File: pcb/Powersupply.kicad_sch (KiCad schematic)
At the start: 37 parts, among them IC3 UCC28910DR, Q3 HL3401A, U3 TPS54202DDC

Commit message: changed capacitors and resistors footprints from 0201 to 0603
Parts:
- C13, C14, C17, C20, C21, C22, C23, C24, C25: footprint Capacitor_SMD:C_0201_0603Metric -> Capacitor_SMD:C_0603_1608Metric
- R16, R17, R23, R24, R26, R27, R33, R34, R35, R36, R37: footprint Resistor_SMD:R_0201_0603Metric -> Resistor_SMD:R_0603_1608Metric
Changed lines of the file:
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@@
 			)
 		)
-		(property "Footprint" "Capacitor_SMD:C_0201_0603Metric"
+		(property "Footprint" "Capacitor_SMD:C_0603_1608Metric"
 			(at 68.2752 163.83 0)
 			(effects
@@
 			)
 		)
-		(property "Footprint" "Capacitor_SMD:C_0201_0603Metric"
+		(property "Footprint" "Capacitor_SMD:C_0603_1608Metric"
 			(at 152.0952 166.37 0)
 			(effects
@@
 			)
 		)
-		(property "Footprint" "Resistor_SMD:R_0201_0603Metric"
+		(property "Footprint" "Resistor_SMD:R_0603_1608Metric"
 			(at 76.962 172.72 90)
 			(effects
@@
 			)
 		)
-		(property "Footprint" "Resistor_SMD:R_0201_0603Metric"
+		(property "Footprint" "Resistor_SMD:R_0603_1608Metric"
 			(at 26.67 160.782 90)
 			(effects
@@
 			)
 		)
-		(property "Footprint" "Resistor_SMD:R_0201_0603Metric"
+		(property "Footprint" "Resistor_SMD:R_0603_1608Metric"
 			(at 76.962 160.02 90)
 			(effects
@@
 			)
 		)
-		(property "Footprint" "Resistor_SMD:R_0201_0603Metric"
+		(property "Footprint" "Resistor_SMD:R_0603_1608Metric"
 			(at 98.552 96.52 90)
 			(effects
@@
 			)
 		)
-		(property "Footprint" "Capacitor_SMD:C_0201_0603Metric"
+		(property "Footprint" "Capacitor_SMD:C_0603_1608Metric"
 			(at 159.7152 176.53 0)
 			(effects
@@
 			)
 		)
-		(property "Footprint" "Resistor_SMD:R_0201_0603Metric"
+		(property "Footprint" "Resistor_SMD:R_0603_1608Metric"
 			(at 165.862 172.72 90)
 			(effects
@@
 			)
 		)
-		(property "Footprint" "Resistor_SMD:R_0201_0603Metric"
+		(property "Footprint" "Resistor_SMD:R_0603_1608Metric"
 			(at 165.862 162.56 90)
 			(effects
@@
 			)
 		)
-		(property "Footprint" "Resistor_SMD:R_0201_0603Metric"
+		(property "Footprint" "Resistor_SMD:R_0603_1608Metric"
 			(at 165.862 182.88 90)
 			(effects
@@
 			)
 		)
-		(property "Footprint" "Resistor_SMD:R_0201_0603Metric"
+		(property "Footprint" "Resistor_SMD:R_0603_1608Metric"
 			(at 29.972 167.64 90)
 			(effects
@@
 			)
 		)
-		(property "Footprint" "Capacitor_SMD:C_0201_0603Metric"
+		(property "Footprint" "Capacitor_SMD:C_0603_1608Metric"
 			(at 121.92 152.7048 0)
 			(effects
@@
 			)
 		)
-		(property "Footprint" "Capacitor_SMD:C_0201_0603Metric"
+		(property "Footprint" "Capacitor_SMD:C_0603_1608Metric"
 			(at 58.1152 163.83 0)
 			(effects
@@
 			)
 		)
-		(property "Footprint" "Capacitor_SMD:C_0201_0603Metric"
+		(property "Footprint" "Capacitor_SMD:C_0603_1608Metric"
 			(at 162.2552 77.47 0)
 			(effects
@@
 			)
 		)
-		(property "Footprint" "Resistor_SMD:R_0201_0603Metric"
+		(property "Footprint" "Resistor_SMD:R_0603_1608Metric"
 			(at 182.372 72.39 90)
 			(effects
@@
 			)
 		)
-		(property "Footprint" "Capacitor_SMD:C_0201_0603Metric"
+		(property "Footprint" "Capacitor_SMD:C_0603_1608Metric"
 			(at 140.6652 166.37 0)
 			(effects
@@
 			)
 		)
-		(property "Footprint" "Resistor_SMD:R_0201_0603Metric"
+		(property "Footprint" "Resistor_SMD:R_0603_1608Metric"
 			(at 223.012 95.25 90)
 			(effects
@@
 			)
 		)
-		(property "Footprint" "Capacitor_SMD:C_0201_0603Metric"
+		(property "Footprint" "Capacitor_SMD:C_0603_1608Metric"
 			(at 201.6252 99.06 0)
 			(effects
@@
 			)
 		)
-		(property "Footprint" "Resistor_SMD:R_0201_0603Metric"
+		(property "Footprint" "Resistor_SMD:R_0603_1608Metric"
 			(at 182.372 55.88 90)
 			(effects
@@
 			)
 		)
-		(property "Footprint" "Capacitor_SMD:C_0201_0603Metric"
+		(property "Footprint" "Capacitor_SMD:C_0603_1608Metric"
 			(at 169.8752 77.47 0)
 			(effects

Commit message: changed SCR drives to pnp drive and started schematic revision
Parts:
- C14: footprint Capacitor_SMD:C_0603_1608Metric -> Capacitor_THT:CP_Radial_D8.0mm_P5.00mm
- C19: footprint Capacitor_SMD:CP_Elec_3x5.4 -> Capacitor_THT:CP_Radial_D8.0mm_P5.00mm
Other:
- note removed: "Aggiungere filtro PiGreco usare calcolatore online"
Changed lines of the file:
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@@
 		)
 	)
-	(text "Aggiungere filtro PiGreco\nusare calcolatore online\n"
-		(exclude_from_sim no)
-		(at 82.296 77.47 0)
-		(effects
-			(font
-				(size 1.27 1.27)
-			)
-		)
-	)
 	(text "simulation"
 		(exclude_from_sim yes)
@@
 			)
 		)
-		(property "Footprint" "Capacitor_SMD:C_0603_1608Metric"
+		(property "Footprint" "Capacitor_THT:CP_Radial_D8.0mm_P5.00mm"
 			(at 162.2552 77.47 0)
 			(effects
@@
 			)
 		)
-		(property "Footprint" "Capacitor_SMD:CP_Elec_3x5.4"
+		(property "Footprint" "Capacitor_THT:CP_Radial_D8.0mm_P5.00mm"
 			(at 214.3252 99.06 0)
 			(effects

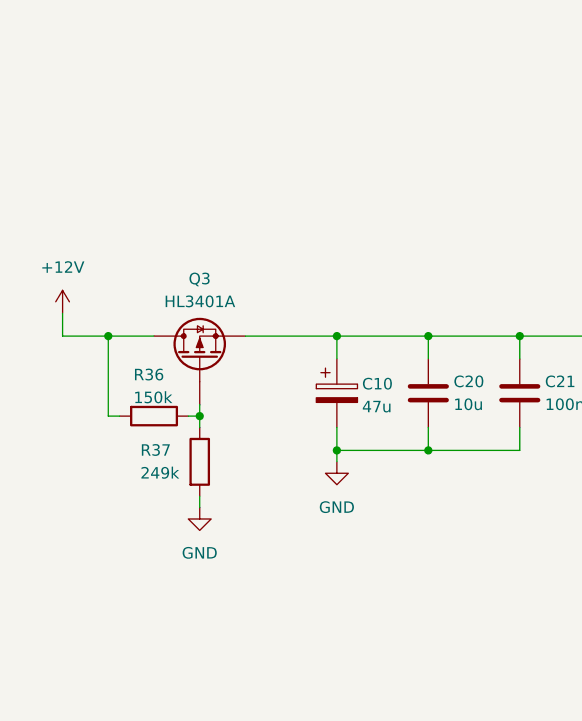
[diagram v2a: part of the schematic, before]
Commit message: fixed reverse polarity protection
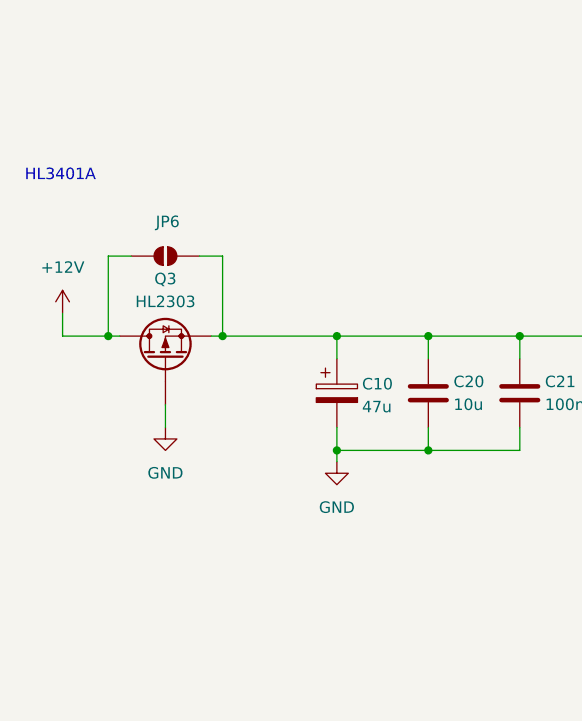
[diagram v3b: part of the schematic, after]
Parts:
- removed R36: 150k, Resistor_SMD:R_0603_1608Metric, symbol Device:R
- removed R37: 249k, Resistor_SMD:R_0603_1608Metric, symbol Device:R
- added JP6: SolderJumper_2_Open, Jumper:SolderJumper-2_P1.3mm_Open_RoundedPad1.0x1.5mm, symbol Jumper:SolderJumper_2_Open
- C10: footprint Capacitor_SMD:CP_Elec_3x5.4 -> Capacitor_THT:CP_Radial_D8.0mm_P5.00mm
- Q3: value HL3401A -> HL2303
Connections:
- net +12V: now also JP6.1 (A)
- net GND: now also Q3.1 (G)
- net at C10.1, C20.1, C21.1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: now also JP6.2 (B)
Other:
- note added: "HL3401A"
- moved on the sheet: Q3

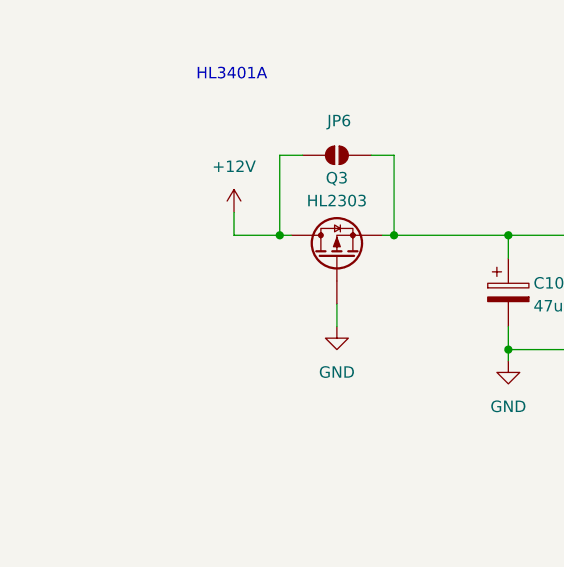
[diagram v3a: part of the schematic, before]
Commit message: added proper handling and comments to QS digital sensor
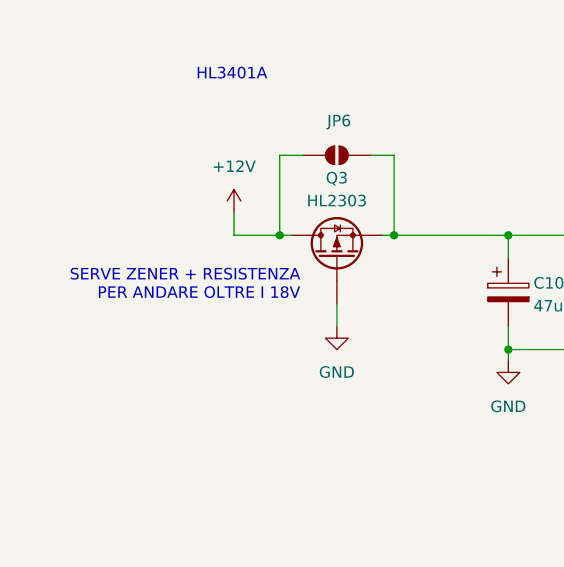
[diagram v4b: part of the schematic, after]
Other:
- note added: "SERVE ZENER + RESISTENZA PER ANDARE OLTRE I 18V"
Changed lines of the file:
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@@
+		)
+	)
+	(text "SERVE ZENER + RESISTENZA\nPER ANDARE OLTRE I 18V\n"
+		(exclude_from_sim no)
+		(at 23.876 159.258 0)
+		(effects
+			(font
+				(size 1.27 1.27)
+			)
+			(justify right)
 		)
 	)

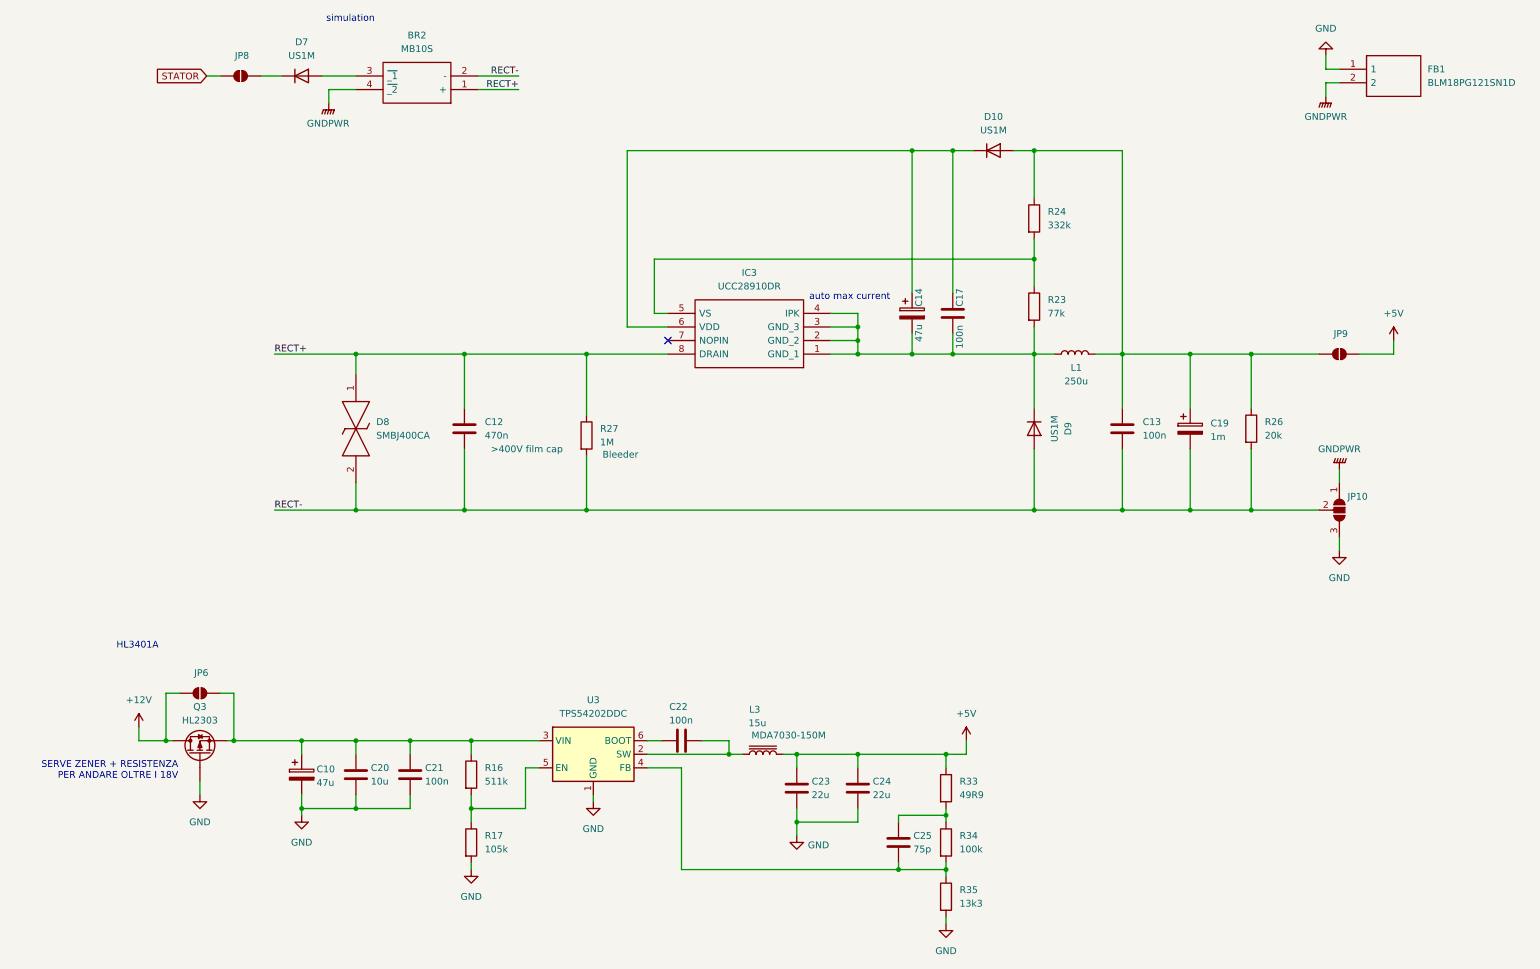
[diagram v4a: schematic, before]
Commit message: changed R and C to standard values
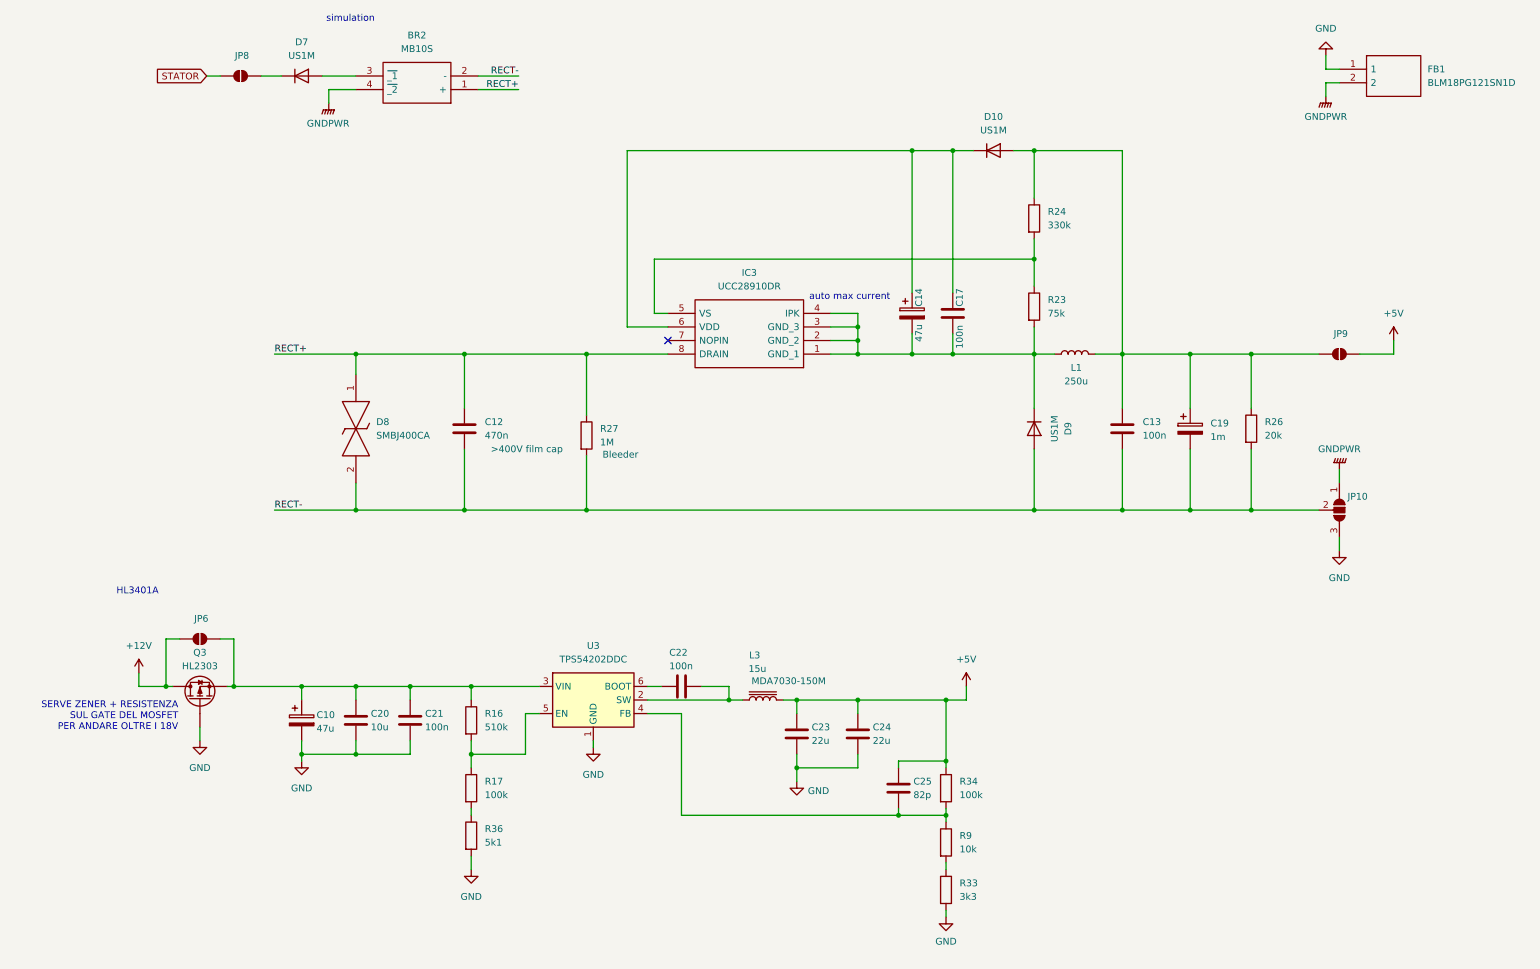
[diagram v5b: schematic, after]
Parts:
- removed R35: 13k3, Resistor_SMD:R_0603_1608Metric, symbol Device:R
- added R36: 5k1, Resistor_SMD:R_0603_1608Metric, symbol Device:R
- added R9: 10k, Resistor_SMD:R_0603_1608Metric, symbol Device:R
- C25: value 75p -> 82p
- R16: value 511k -> 510k
- R17: value 105k -> 100k
- R23: value 77k -> 75k
- R24: value 332k -> 330k
- R33: value 49R9 -> 3k3
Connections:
- net +5V: now also C25.1, R34.1; no longer R33.1
- net GND: now also R33.2, R36.2; no longer R17.2
- net at C25.2, R34.2, U3.4 (FB): now also R9.1
- new net: R17.2, R36.1
- new net: R33.1, R9.2
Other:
- note added: "SERVE ZENER + RESISTENZA SUL GATE DEL MOSFET PER ANDARE OLTRE I 18V"
- note removed: "SERVE ZENER + RESISTENZA PER ANDARE OLTRE I 18V"
- moved on the sheet: C10, C20, C21, C22, C23, C24, C25, JP6, L3, Q3, R16, R17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
